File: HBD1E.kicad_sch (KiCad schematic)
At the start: 62 parts, among them J1 Conn_01x08_Male, Q1 C3M0030090K, Q2 C3M0030090K, U1 UCC21520DW, U2 LM317_SOT-223, U3 3S7B-2424S3UP, U4 LM317_SOT-223, U5 3S7B-2424S3UP

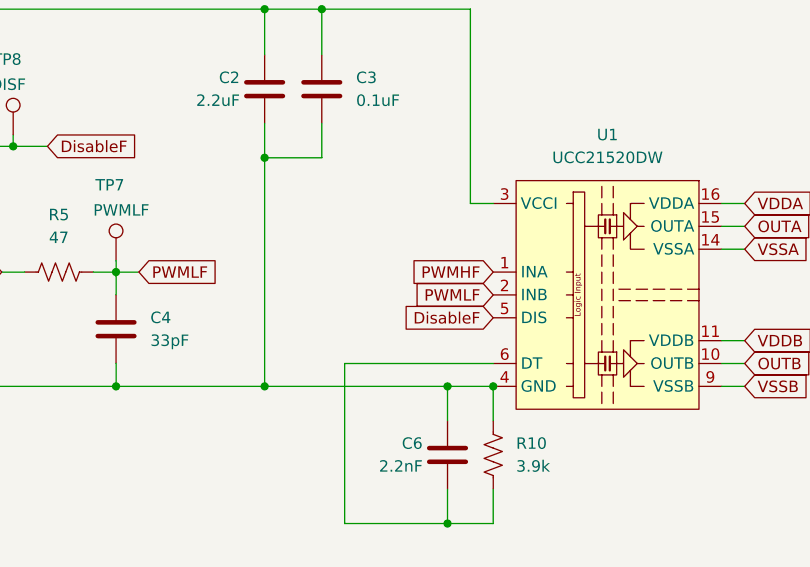
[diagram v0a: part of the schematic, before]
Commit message: Added a pull-up resistor for dead time configuration.
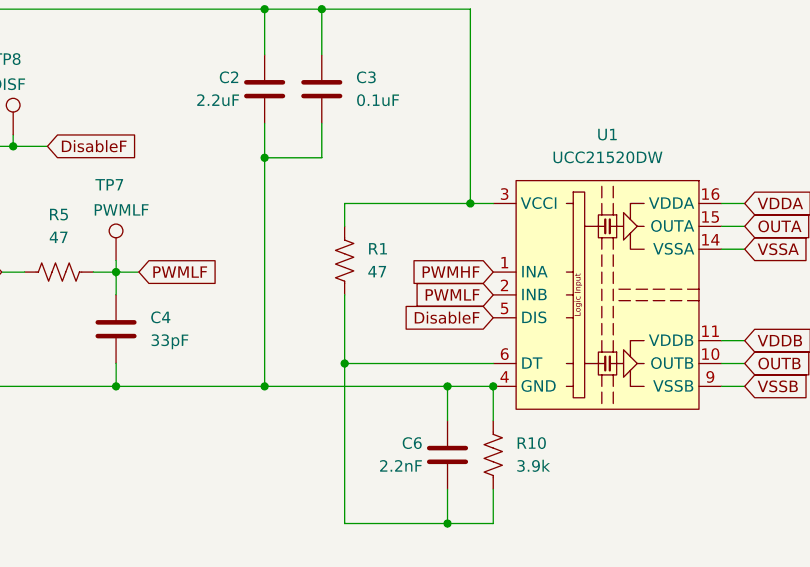
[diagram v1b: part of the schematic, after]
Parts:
- added R1: 47, Resistor_SMD:R_0805_2012Metric_Pad1.20x1.40mm_HandSolder, symbol Device:R_US
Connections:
- net Vcc: now also R1.2
- net at C6.2, R10.1, U1.6 (DT): now also R1.1
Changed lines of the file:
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@@
 	)
 	(junction
+		(at 135.89 66.04)
+		(diameter 0)
+		(color 0 0 0 0)
+	)
+	(junction
 		(at 97.79 120.65)
 		(diameter 0)
@@
 	)
 	(junction
+		(at 149.86 48.26)
+		(diameter 0)
+		(color 0 0 0 0)
+	)
+	(junction
 		(at 147.32 83.82)
 		(diameter 0)
@@
 	(wire
 		(pts
+			(xy 135.89 48.26) (xy 149.86 48.26)
+		)
+		(stroke
+			(width 0)
+			(type default)
+		)
+	)
+	(wire
+		(pts
 			(xy 110.49 66.04) (xy 110.49 68.58)
 		)
@@
 	(wire
 		(pts
+			(xy 135.89 58.42) (xy 135.89 66.04)
+		)
+		(stroke
+			(width 0)
+			(type default)
+		)
+	)
+	(wire
+		(pts
 			(xy 222.25 139.7) (xy 203.2 139.7)
 		)
@@
 	(wire
 		(pts
+			(xy 135.89 50.8) (xy 135.89 48.26)
+		)
+		(stroke
+			(width 0)
+			(type default)
+		)
+	)
+	(wire
+		(pts
 			(xy 246.38 110.49) (xy 246.38 105.41)
 		)
@@
 					(unit 1)
 				)
+			)
+		)
+	)
+	(symbol
+		(lib_id "Device:R_US")
+		(at 135.89 54.61 180)
+		(unit 1)
+		(exclude_from_sim no)
+		(in_bom yes)
+		(on_board yes)
+		(dnp no)
+		(fields_autoplaced yes)
+		(property "Reference" "R1"
+			(at 138.43 53.3399 0)
+			(effects
+				(font
+					(size 1.27 1.27)
+				)
+				(justify right)
+			)
+		)
+		(property "Value" "47"
+			(at 138.43 55.8799 0)
+			(effects
+				(font
+					(size 1.27 1.27)
+				)
+				(justify right)
+			)
+		)
+		(property "Footprint" "Resistor_SMD:R_0805_2012Metric_Pad1.20x1.40mm_HandSolder"
+			(at 134.874 54.356 90)
+			(effects
+				(font
+					(size 1.27 1.27)
+				)
+				(hide yes)
+			)
+		)
+		(property "Datasheet" "~"
+			(at 135.89 54.61 0)
+			(effects
+				(font
+					(size 1.27 1.27)
+				)
+				(hide yes)
+			)
+		)
+		(property "Description" ""
+			(at 135.89 54.61 0)
+			(effects
+				(font
+					(size 1.27 1.27)
+				)
+				(hide yes)
+			)
+		)
+		(pin "1"
+		)
+		(pin "2"
+		)
+		(instances
+			(project "HBD1E"
+				(path "/38c37fb8-112f-467b-a525-6bd471bac216"
+					(reference "R1")
+					(unit 1)
+				)
